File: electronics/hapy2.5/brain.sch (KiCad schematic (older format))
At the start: 30 parts, among them P10 WTemp probe, P11 UPPER_BED, P15 Air probe, P19 Power button, P20 T821126A1S100CEU HE10-26, P4 PH Probe, P5 Tank Level Sensor, P6 UPPER_LEDS, P7 LOWER_LEDS, P8 USER_PANEL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

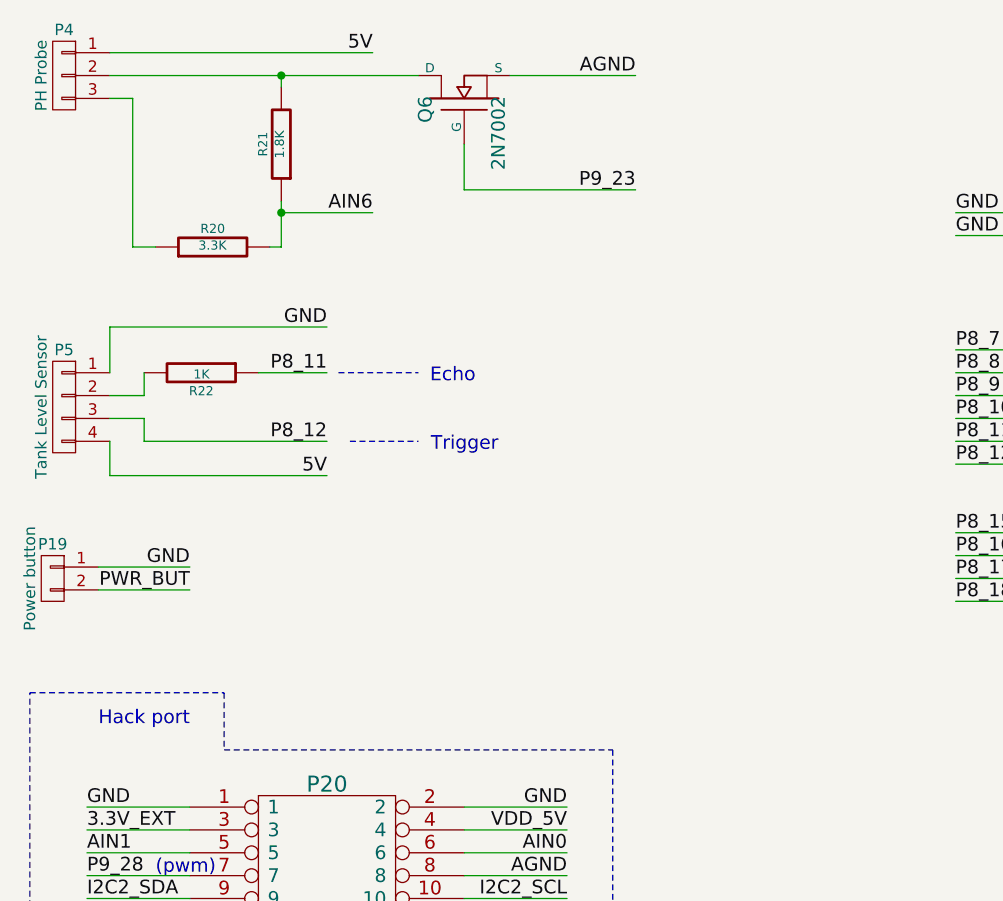
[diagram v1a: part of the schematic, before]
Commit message: enhanced schema and more room around ph probe slot
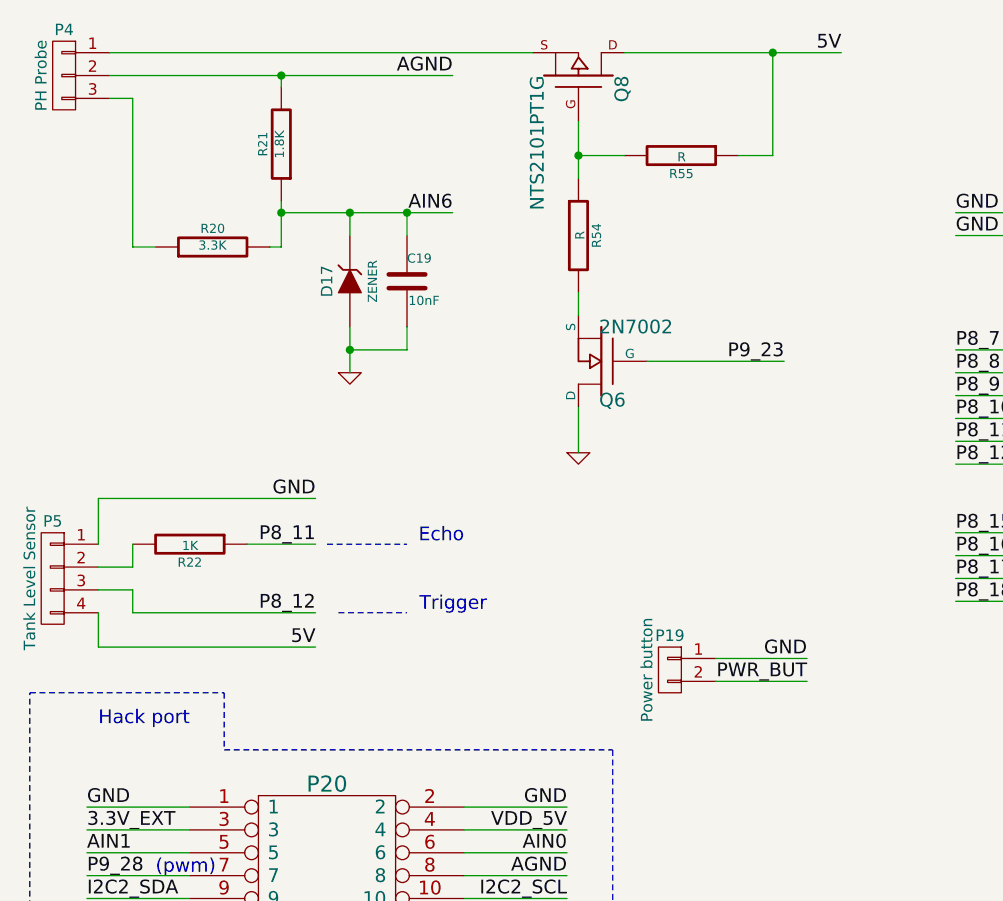
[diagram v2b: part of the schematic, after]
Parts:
- added C19: 10nF, symbol C
- added D17: ZENER, symbol ZENER
- added Q8: NTS2101PT1G, symbol MOS_P
- added R54, R55: R, symbol R
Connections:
- net 5V: now also Q8.D, R55.1; no longer P4.1 (P1)
- net AGND: now also P4.2 (P2), R21.2; no longer Q6.S
- net AIN6: now also C19.1, D17.2 (K)
- net GND: now also Q6.D, C19.2, D17.1 (A)
- new net: P4.1 (P1), Q8.S
- new net: Q6.S, R54.2
- new net: Q8.G, R54.1, R55.2
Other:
- moved on the sheet: P19, P5, Q6, R22
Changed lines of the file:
@@
 L R R22
 U 1 1 55F2AE59
-P 1550 2150
-F 0 "R22" V 1630 2150 40  0000 C CNN
-F 1 "1K" V 1557 2151 40  0000 C CNN
-F 2 "Resistors_SMD:R_0603" V 1480 2150 30  0001 C CNN
-F 3 "" H 1550 2150 30  0000 C CNN
-	1    1550 2150
+P 1500 2900
+F 0 "R22" V 1580 2900 40  0000 C CNN
+F 1 "1K" V 1507 2901 40  0000 C CNN
+F 2 "Resistors_SMD:R_0603" V 1430 2900 30  0001 C CNN
+F 3 "" H 1500 2900 30  0000 C CNN
+	1    1500 2900
 	0    1    1    0
 $EndComp
@@
 L CONN_01X04 P5
 U 1 1 55F2AE60
-P 950 2300
-F 0 "P5" H 950 2550 50  0000 C CNN
-F 1 "Tank Level Sensor" V 1050 2300 50  0000 C CNN
-F 2 "smisioto_bornier_mpt:mpt_0,5%2f4-2,54" H 950 2300 60  0001 C CNN
-F 3 "" H 950 2300 60  0000 C CNN
-	1    950  2300
+P 900 3050
+F 0 "P5" H 900 3300 50  0000 C CNN
+F 1 "Tank Level Sensor" V 1000 3050 50  0000 C CNN
+F 2 "smisioto_bornier_mpt:mpt_0,5%2f4-2,54" H 900 3050 60  0001 C CNN
+F 3 "" H 900 3050 60  0000 C CNN
+	1    900  3050
 	-1   0    0    -1
 $EndComp
-Text Label 2100 2600 2    60   ~ 0
+Text Label 2050 3350 2    60   ~ 0
 5V
-Text Label 2100 2450 2    60   ~ 0
+Text Label 2050 3200 2    60   ~ 0
 P8_12
-Text Label 2100 2150 2    60   ~ 0
+Text Label 2050 2900 2    60   ~ 0
 P8_11
-Text Label 2100 1950 2    60   ~ 0
-GND
-Text Label 2300 750  2    60   ~ 0
-5V
-Text Label 3450 850  2    60   ~ 0
+Text Label 2050 2700 2    60   ~ 0
+GND
+Text Label 2650 850  2    60   ~ 0
 AGND
-Text Label 2300 1450 2    60   ~ 0
+Text Label 2650 1450 2    60   ~ 0
 AIN6
 Text HLabel 1600 6350 0    60   Input ~ 0
@@
 5V
 $Comp
-L GND #PWR035
+L GND #PWR019
 U 1 1 55F3CF20
 P 1250 7500
-F 0 "#PWR035" H 1250 7500 30  0001 C CNN
+F 0 "#PWR019" H 1250 7500 30  0001 C CNN
 F 1 "GND" H 1250 7430 30  0001 C CNN
 F 2 "" H 1250 7500 60  0000 C CNN
@@
 Text Label 7100 5550 2    60   ~ 0
 P9_42
-Text Notes 2750 2200 2    60   ~ 0
+Text Notes 2700 2900 2    60   ~ 0
 Echo
-Text Notes 2850 2500 2    60   ~ 0
+Text Notes 2800 3200 2    60   ~ 0
 Trigger
 Text Label 7100 5650 2    60   ~ 0
@@
 L CONN_01X02 P19
 U 1 1 55FB4E48
-P 900 3050
-F 0 "P19" H 900 3200 50  0000 C CNN
-F 1 "Power button" V 1000 3050 50  0000 C CNN
-F 2 "smisioto_bornier_mpt:mpt_0,5%2f2-2,54" H 900 3050 60  0001 C CNN
-F 3 "" H 900 3050 60  0000 C CNN
-	1    900  3050
+P 3600 3450
+F 0 "P19" H 3600 3600 50  0000 C CNN
+F 1 "Power button" V 3700 3450 50  0000 C CNN
+F 2 "smisioto_bornier_mpt:mpt_0,5%2f2-2,54" H 3600 3450 60  0001 C CNN
+F 3 "" H 3600 3450 60  0000 C CNN
+	1    3600 3450
 	-1   0    0    -1
 $EndComp
-Text Label 1500 3000 2    60   ~ 0
-GND
-Text Label 1500 3100 2    60   ~ 0
+Text Label 4200 3400 2    60   ~ 0
+GND
+Text Label 4200 3500 2    60   ~ 0
 PWR_BUT
 Text Label 7100 3650 2    60   ~ 0
@@
 L MOS_N Q6
 U 1 1 55FB58DE
-P 2700 950
-F 0 "Q6" H 2710 1120 60  0000 R CNN
-F 1 "2N7002" H 2710 800 60  0000 R CNN
-F 2 "risebox:SOT-23-FET" H 2700 950 60  0001 C CNN
-F 3 "" H 2700 950 60  0000 C CNN
-	1    2700 950
-	0    -1   -1   0
-$EndComp
-Text Label 3450 1350 2    60   ~ 0
+P 3300 2100
+F 0 "Q6" H 3310 2270 60  0000 R CNN
+F 1 "2N7002" H 3310 1950 60  0000 R CNN
+F 2 "risebox:SOT-23-FET" H 3300 2100 60  0001 C CNN
+F 3 "" H 3300 2100 60  0000 C CNN
+	1    3300 2100
+	-1   0    0    1
+$EndComp
+Text Label 4100 2100 2    60   ~ 0
 P9_23
 Text HLabel 1600 6550 0    60   Input ~ 0
@@
 	6700 3650 7100 3650
 Wire Wire Line
-	1100 3000 1500 3000
-Wire Wire Line
-	1100 3100 1500 3100
+	3800 3400 4200 3400
+Wire Wire Line
+	3800 3500 4200 3500
 Wire Wire Line
 	5200 4550 4850 4550
@@
 	9700 6150 9350 6150
 Wire Wire Line
-	1150 2350 1300 2350
-Wire Wire Line
-	1300 2350 1300 2450
-Wire Wire Line
-	1300 2450 2100 2450
-Wire Wire Line
-	1150 2250 1300 2250
-Wire Wire Line
-	1300 2250 1300 2150
-Wire Wire Line
-	1800 2150 2100 2150
-Wire Wire Line
-	1150 2450 1150 2600
-Wire Wire Line
-	1150 2600 2100 2600
-Wire Wire Line
-	1150 1950 1150 2150
-Wire Wire Line
-	1150 1950 2100 1950
-Wire Wire Line
-	1150 750  2300 750
-Wire Wire Line
-	1150 850  2500 850
+	1100 3100 1250 3100
+Wire Wire Line
+	1250 3100 1250 3200
+Wire Wire Line
+	1250 3200 2050 3200
+Wire Wire Line
+	1100 3000 1250 3000
+Wire Wire Line
+	1250 3000 1250 2900
+Wire Wire Line
+	1750 2900 2050 2900
+Wire Wire Line
+	1100 3200 1100 3350
+Wire Wire Line
+	1100 3350 2050 3350
+Wire Wire Line
+	1100 2700 1100 2900
+Wire Wire Line
+	1100 2700 2050 2700
+Wire Wire Line
+	1150 850  2650 850
 Wire Wire Line
 	1150 950  1250 950
@@
 	1900 1400 1900 1600
 Wire Wire Line
-	1900 1450 2300 1450
+	1900 1450 2650 1450
 Connection ~ 1900 1450
 Wire Wire Line
@@
 	6700 5550 7100 5550
 Wire Notes Line
-	2150 2150 2500 2150
-Wire Notes Line
-	2200 2450 2500 2450
+	2100 2900 2450 2900
+Wire Notes Line
+	2150 3200 2450 3200
 Wire Wire Line
 	5200 1450 4850 1450
@@
 	3400 6500 3850 6500
 Wire Wire Line
-	2900 850  3450 850
-Wire Wire Line
-	2700 1150 2700 1350
-Wire Wire Line
-	2700 1350 3450 1350
+	3500 2100 4100 2100
 Wire Wire Line
 	1600 6550 2050 6550
@@
 NoConn ~ 5200 5650
 NoConn ~ 5100 5000
+$Comp
+L ZENER D17
+U 1 1 560BEB1E
+P 2200 1750
+F 0 "D17" H 2200 1850 50  0000 C CNN
+F 1 "ZENER" H 2200 1650 40  0000 C CNN
+F 2 "" H 2200 1750 60  0000 C CNN
+F 3 "" H 2200 1750 60  0000 C CNN
+	1    2200 1750
+	0    -1   -1   0
+$EndComp
+Wire Wire Line
+	2200 1550 2200 1450
+Wire Wire Line
+	2200 1950 2200 2150
+$Comp
+L GND #PWR020
+U 1 1 560BEEB4
+P 2200 2150
+F 0 "#PWR020" H 2200 2150 30  0001 C CNN
+F 1 "GND" H 2200 2080 30  0001 C CNN
+F 2 "" H 2200 2150 60  0000 C CNN
+F 3 "" H 2200 2150 60  0000 C CNN
+	1    2200 2150
+	1    0    0    -1
+$EndComp
+$Comp
+L MOS_P Q8
+U 1 1 560BF63D
+P 3200 850
+F 0 "Q8" H 3200 1040 60  0000 R CNN
+F 1 "NTS2101PT1G" H 3200 670 60  0000 R CNN
+F 2 "" H 3200 850 60  0000 C CNN
+F 3 "" H 3200 850 60  0000 C CNN
+	1    3200 850
+	0    1    -1   0
+$EndComp
+Wire Wire Line
+	3400 750  4350 750
+Text Label 4350 750  2    60   ~ 0
+5V
+Wire Wire Line
+	3200 2300 3200 2500
+$Comp
+L GND #PWR021
+U 1 1 560C0052
+P 3200 2500
+F 0 "#PWR021" H 3200 2500 30  0001 C CNN
+F 1 "GND" H 3200 2430 30  0001 C CNN
+F 2 "" H 3200 2500 60  0000 C CNN
+F 3 "" H 3200 2500 60  0000 C CNN
+	1    3200 2500
+	1    0    0    -1
+$EndComp
+$Comp
+L R R55
+U 1 1 560C0066
+P 3650 1200
+F 0 "R55" V 3730 1200 40  0000 C CNN
+F 1 "R" V 3657 1201 40  0000 C CNN
+F 2 "" V 3580 1200 30  0000 C CNN
+F 3 "" H 3650 1200 30  0000 C CNN
+	1    3650 1200
+	0    1    1    0
+$EndComp
+Wire Wire Line
+	4050 750  4050 1200
+Wire Wire Line
+	4050 1200 3900 1200
+Connection ~ 4050 750
+Wire Wire Line
+	3200 1050 3200 1300
+Wire Wire Line
+	3200 1200 3400 1200
+$Comp
+L R R54
+U 1 1 560C072C
+P 3200 1550
+F 0 "R54" V 3280 1550 40  0000 C CNN
+F 1 "R" V 3207 1551 40  0000 C CNN
+F 2 "" V 3130 1550 30  0000 C CNN
+F 3 "" H 3200 1550 30  0000 C CNN
+	1    3200 1550
+	1    0    0    -1
+$EndComp
+Connection ~ 3200 1200
+Wire Wire Line
+	3200 1800 3200 1900
+Connection ~ 2200 1450
+Wire Wire Line
+	1150 750  3000 750
+$Comp
+L C C19
+U 1 1 560C1319
+P 2450 1750
+F 0 "C19" H 2450 1850 40  0000 L CNN
+F 1 "10nF" H 2456 1665 40  0000 L CNN
+F 2 "" H 2488 1600 30  0000 C CNN
+F 3 "" H 2450 1750 60  0000 C CNN
+	1    2450 1750
+	1    0    0    -1
+$EndComp
+Wire Wire Line
+	2450 1950 2450 2050
+Wire Wire Line
+	2450 2050 2200 2050
+Connection ~ 2200 2050
+Wire Wire Line
+	2450 1550 2450 1450
+Connection ~ 2450 1450
 $EndSCHEMATC

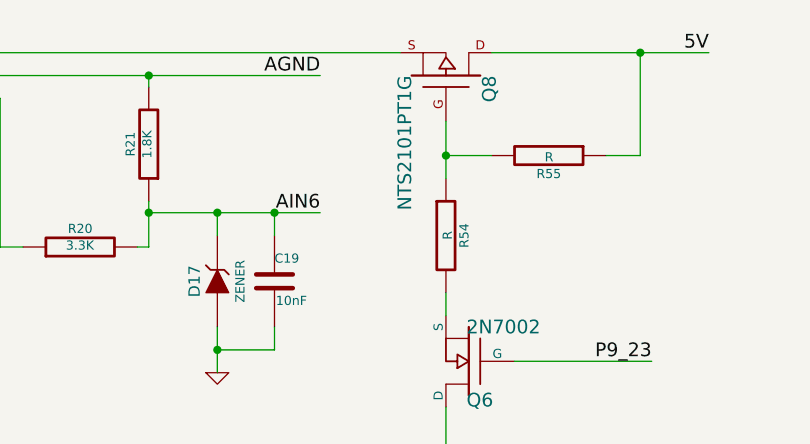
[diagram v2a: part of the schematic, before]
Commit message: fix footprints
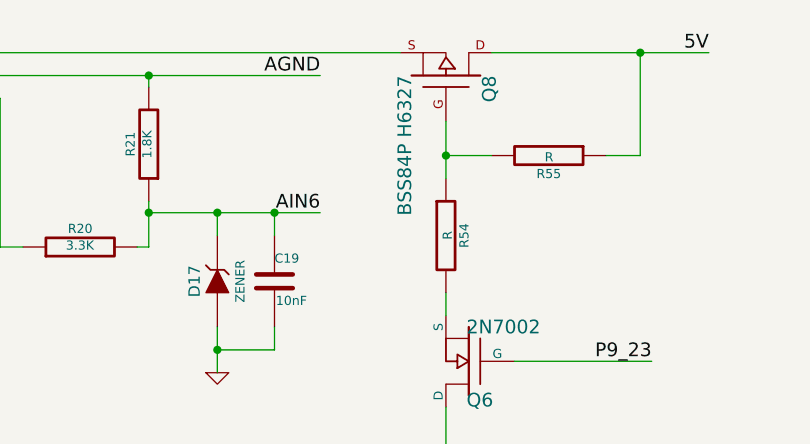
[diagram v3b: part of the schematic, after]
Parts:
- C19: footprint (none) -> Capacitors_SMD:C_0402
- D17: footprint (none) -> risebox:DIODE_SOD-123
- Q8: value NTS2101PT1G -> BSS84P H6327; footprint (none) -> risebox:SOT-23-FET
- R54, R55: footprint (none) -> Resistors_SMD:R_0603
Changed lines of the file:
@@
 F 0 "D17" H 2200 1850 50  0000 C CNN
 F 1 "ZENER" H 2200 1650 40  0000 C CNN
-F 2 "" H 2200 1750 60  0000 C CNN
+F 2 "risebox:DIODE_SOD-123" H 2200 1750 60  0001 C CNN
 F 3 "" H 2200 1750 60  0000 C CNN
 	1    2200 1750
@@
 P 3200 850
 F 0 "Q8" H 3200 1040 60  0000 R CNN
-F 1 "NTS2101PT1G" H 3200 670 60  0000 R CNN
-F 2 "" H 3200 850 60  0000 C CNN
+F 1 "BSS84P H6327" H 3200 670 60  0000 R CNN
+F 2 "risebox:SOT-23-FET" H 3200 850 60  0001 C CNN
 F 3 "" H 3200 850 60  0000 C CNN
 	1    3200 850
@@
 F 0 "R55" V 3730 1200 40  0000 C CNN
 F 1 "R" V 3657 1201 40  0000 C CNN
-F 2 "" V 3580 1200 30  0000 C CNN
+F 2 "Resistors_SMD:R_0603" V 3580 1200 30  0001 C CNN
 F 3 "" H 3650 1200 30  0000 C CNN
 	1    3650 1200
@@
 F 0 "R54" V 3280 1550 40  0000 C CNN
 F 1 "R" V 3207 1551 40  0000 C CNN
-F 2 "" V 3130 1550 30  0000 C CNN
+F 2 "Resistors_SMD:R_0603" V 3130 1550 30  0001 C CNN
 F 3 "" H 3200 1550 30  0000 C CNN
 	1    3200 1550
@@
 F 0 "C19" H 2450 1850 40  0000 L CNN
 F 1 "10nF" H 2456 1665 40  0000 L CNN
-F 2 "" H 2488 1600 30  0000 C CNN
+F 2 "Capacitors_SMD:C_0402" H 2488 1600 30  0001 C CNN
 F 3 "" H 2450 1750 60  0000 C CNN
 	1    2450 1750

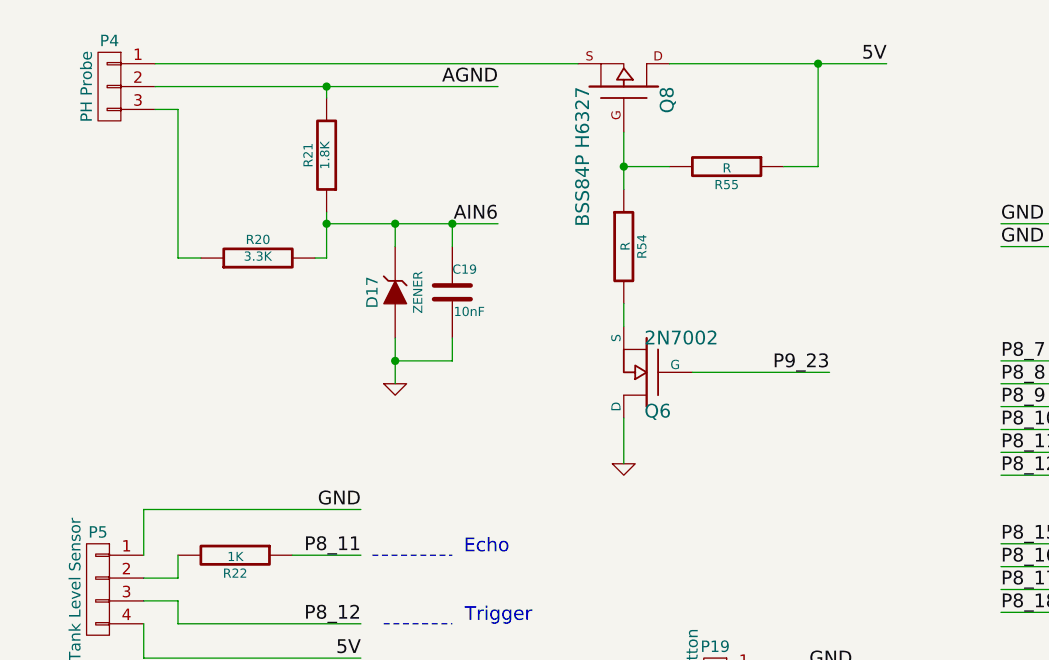
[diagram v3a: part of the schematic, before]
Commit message: changed schema to reflect proper ph probe pin order
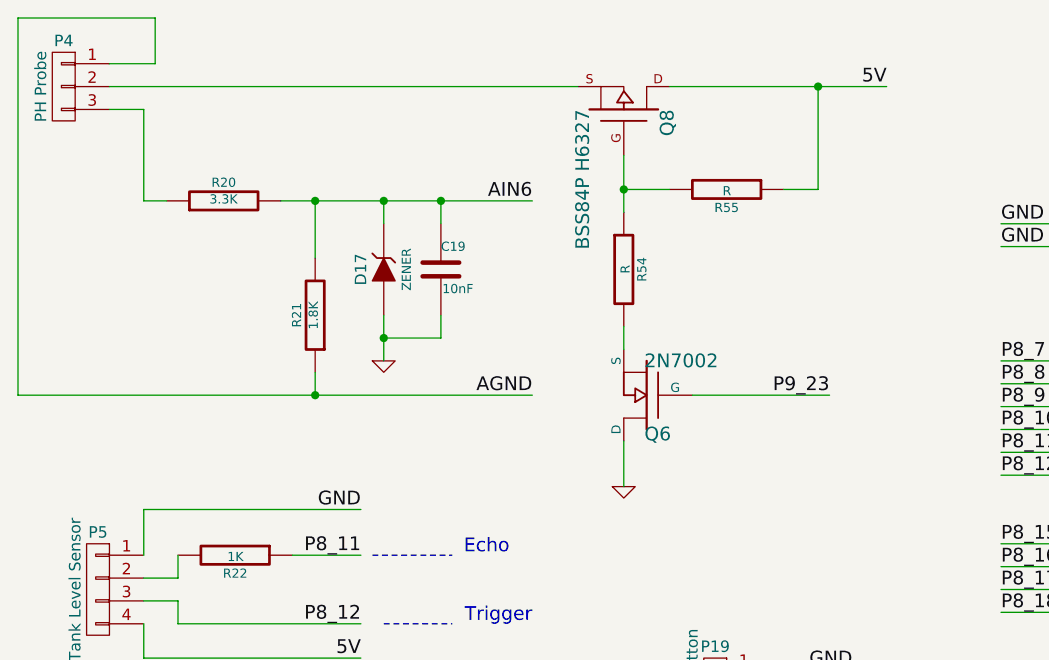
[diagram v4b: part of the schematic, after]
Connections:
- net AGND: now also P4.1 (P1), R21.1; no longer P4.2 (P2), R21.2
- net AIN6: now also R21.2; no longer R21.1
- net at Q8.S: now also P4.2 (P2); no longer P4.1 (P1)
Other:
- moved on the sheet: C19, D17, P4, Q6, Q8, R20, R21, R54, R55

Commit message: post crafty review, wip
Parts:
- added C? (x2): 0.1µF, symbol C
- added R56: 10K, symbol R
- added R57: 100, symbol R
- R54: value R -> 100
- R55: value R -> 10K
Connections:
- net 3.3Vout: now also C?.1, C?.1
- net GND: now also C?.2, C?.2, R56.2
- net P9_23: now also R57.1; no longer Q6.G
- new net: Q6.G, R56.1, R57.2
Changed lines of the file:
@@
 5V
 $Comp
-L GND #PWR019
+L GND #PWR19
 U 1 1 55F3CF20
 P 1250 7500
-F 0 "#PWR019" H 1250 7500 30  0001 C CNN
+F 0 "#PWR19" H 1250 7500 30  0001 C CNN
 F 1 "GND" H 1250 7430 30  0001 C CNN
 F 2 "" H 1250 7500 60  0000 C CNN
@@
 	-1   0    0    1
 $EndComp
-Text Label 4100 2200 2    60   ~ 0
+Text Label 4650 2200 2    60   ~ 0
 P9_23
 Text HLabel 1600 6550 0    60   Input ~ 0
@@
 $EndComp
 $Comp
-L GND #PWR020
+L GND #PWR20
 U 1 1 560BEEB4
 P 2150 2050
-F 0 "#PWR020" H 2150 2050 30  0001 C CNN
+F 0 "#PWR20" H 2150 2050 30  0001 C CNN
 F 1 "GND" H 2150 1980 30  0001 C CNN
 F 2 "" H 2150 2050 60  0000 C CNN
@@
 5V
 $Comp
-L GND #PWR021
+L GND #PWR21
 U 1 1 560C0052
 P 3200 2600
-F 0 "#PWR021" H 3200 2600 30  0001 C CNN
+F 0 "#PWR21" H 3200 2600 30  0001 C CNN
 F 1 "GND" H 3200 2530 30  0001 C CNN
 F 2 "" H 3200 2600 60  0000 C CNN
@@
 P 3650 1300
 F 0 "R55" V 3730 1300 40  0000 C CNN
-F 1 "R" V 3657 1301 40  0000 C CNN
+F 1 "10K" V 3657 1301 40  0000 C CNN
 F 2 "Resistors_SMD:R_0603" V 3580 1300 30  0001 C CNN
 F 3 "" H 3650 1300 30  0000 C CNN
@@
 P 3200 1650
 F 0 "R54" V 3280 1650 40  0000 C CNN
-F 1 "R" V 3207 1651 40  0000 C CNN
+F 1 "100" V 3207 1651 40  0000 C CNN
 F 2 "Resistors_SMD:R_0603" V 3130 1650 30  0001 C CNN
 F 3 "" H 3200 1650 30  0000 C CNN
@@
 	7600 5300 8100 5300
 Wire Wire Line
-	7600 4800 8100 4800
+	7400 4800 8100 4800
 Wire Wire Line
 	7650 2650 8150 2650
@@
 	7650 3250 8150 3250
 Wire Wire Line
-	7650 2750 8150 2750
+	7450 2750 8150 2750
 Wire Wire Line
 	10400 6050 10150 6050
@@
 	3400 6500 3850 6500
 Wire Wire Line
-	3500 2200 4100 2200
+	3500 2200 3800 2200
 Wire Wire Line
 	1600 6550 2050 6550
@@
 Wire Wire Line
 	1150 750  950  750
+Wire Wire Line
+	3650 2200 3650 2300
+Connection ~ 3650 2200
+$Comp
+L R R56
+U 1 1 560DD0DF
+P 3650 2550
+F 0 "R56" V 3730 2550 40  0000 C CNN
+F 1 "10K" V 3657 2551 40  0000 C CNN
+F 2 "" V 3580 2550 30  0000 C CNN
+F 3 "" H 3650 2550 30  0000 C CNN
+	1    3650 2550
+	1    0    0    -1
+$EndComp
+Wire Wire Line
+	3650 2800 3650 2900
+$Comp
+L GND #PWR22
+U 1 1 560DD230
+P 3650 2900
+F 0 "#PWR22" H 3650 2900 30  0001 C CNN
+F 1 "GND" H 3650 2830 30  0001 C CNN
+F 2 "" H 3650 2900 60  0000 C CNN
+F 3 "" H 3650 2900 60  0000 C CNN
+	1    3650 2900
+	1    0    0    -1
+$EndComp
+$Comp
+L R R57
+U 1 1 560DD2EA
+P 4050 2200
+F 0 "R57" V 4130 2200 40  0000 C CNN
+F 1 "100" V 4057 2201 40  0000 C CNN
+F 2 "" V 3980 2200 30  0000 C CNN
+F 3 "" H 4050 2200 30  0000 C CNN
+	1    4050 2200
+	0    1    1    0
+$EndComp
+Wire Wire Line
+	4300 2200 4650 2200
+$Comp
+L C C?
+U 1 1 560DEF2B
+P 7450 3150
+F 0 "C?" H 7450 3250 40  0000 L CNN
+F 1 "0.1µF" H 7456 3065 40  0000 L CNN
+F 2 "" H 7488 3000 30  0000 C CNN
+F 3 "" H 7450 3150 60  0000 C CNN
+	1    7450 3150
+	1    0    0    -1
+$EndComp
+$Comp
+L C C?
+U 1 1 560DEF5E
+P 7400 5200
+F 0 "C?" H 7400 5300 40  0000 L CNN
+F 1 "0.1µF" H 7406 5115 40  0000 L CNN
+F 2 "" H 7438 5050 30  0000 C CNN
+F 3 "" H 7400 5200 60  0000 C CNN
+	1    7400 5200
+	1    0    0    -1
+$EndComp
+Wire Wire Line
+	7400 4800 7400 5000
+Wire Wire Line
+	7400 5400 7400 5600
+$Comp
+L GND #PWR?
+U 1 1 560DF36B
+P 7400 5600
+F 0 "#PWR?" H 7400 5600 30  0001 C CNN
+F 1 "GND" H 7400 5530 30  0001 C CNN
+F 2 "" H 7400 5600 60  0000 C CNN
+F 3 "" H 7400 5600 60  0000 C CNN
+	1    7400 5600
+	1    0    0    -1
+$EndComp
+Wire Wire Line
+	7450 2750 7450 2950
+Wire Wire Line
+	7450 3350 7450 3550
+$Comp
+L GND #PWR?
+U 1 1 560DF7DC
+P 7450 3550
+F 0 "#PWR?" H 7450 3550 30  0001 C CNN
+F 1 "GND" H 7450 3480 30  0001 C CNN
+F 2 "" H 7450 3550 60  0000 C CNN
+F 3 "" H 7450 3550 60  0000 C CNN
+	1    7450 3550
+	1    0    0    -1
+$EndComp
 $EndSCHEMATC
